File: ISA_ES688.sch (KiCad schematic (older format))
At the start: 106 parts, among them J1 LINE IN, J11 ISA BUS, J2 LINE OUT, J3 Joystick/MIDI, J7 SPKR OUT, J8 MIC, U1 L78L05, U2 74LS14, U7 LM1877, Y1 14.318Mhz

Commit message: Completed OPAMP circuit?
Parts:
- added C28: 5nF, Capacitor_THT:C_Disc_D6.0mm_W2.5mm_P5.00mm, symbol Device:C_Small
- added C29: 2.7nF, Capacitor_THT:C_Disc_D6.0mm_W2.5mm_P5.00mm, symbol Device:C_Small
- added R2, R3: 10k, Resistor_THT:R_Axial_DIN0207_L6.3mm_D2.5mm_P7.62mm_Horizontal, symbol Device:R_Small
- added R4: 2.2k, Resistor_THT:R_Axial_DIN0207_L6.3mm_D2.5mm_P7.62mm_Horizontal, symbol Device:R_Small
- gave numbers to parts that had none: 1
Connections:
- net GNDA: now also C28.2, C29.2
- net MUS_L: now also C28.1, R4.2
- net YAC_CH2: now also U?.10 (IN+), C29.1
- net YAC_MP: now also R6.2, R3.2; no longer R6.1
- net at U?.8 (OUT): now also R2.1, R4.1
- net at U?.9 (IN-): now also R2.2, R3.1
- net at R5.2, U?.13 (IN-): now also R6.1; no longer R6.2
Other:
- moved on the sheet: C26, R1, R6, U?B, U?C
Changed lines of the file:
@@
 L custom_components:LM3403 U?
 U 2 1 618ABB59
-P 19950 11550
-F 0 "U?" H 19750 11850 50  0000 L CNN
-F 1 "LM3403" H 19950 11850 50  0000 L CNN
-F 2 "" H 19950 11550 50  0001 C CNN
-F 3 "" H 19950 11550 50  0001 C CNN
-	2    19950 11550
+P 19950 13500
+F 0 "U?" H 19750 13800 50  0000 L CNN
+F 1 "LM3403" H 19950 13800 50  0000 L CNN
+F 2 "" H 19950 13500 50  0001 C CNN
+F 3 "" H 19950 13500 50  0001 C CNN
+	2    19950 13500
 	1    0    0    -1
 $EndComp
@@
 L custom_components:LM3403 U?
 U 3 1 6191F91E
-P 19950 12500
-F 0 "U?" H 19750 12800 50  0000 L CNN
-F 1 "LM3403" H 19950 12800 50  0000 L CNN
-F 2 "" H 19950 12500 50  0001 C CNN
-F 3 "" H 19950 12500 50  0001 C CNN
-	3    19950 12500
-	1    0    0    -1
+P 19900 11400
+F 0 "U?" H 19700 11700 50  0000 L CNN
+F 1 "LM3403" H 19900 11700 50  0000 L CNN
+F 2 "" H 19900 11400 50  0001 C CNN
+F 3 "" H 19900 11400 50  0001 C CNN
+	3    19900 11400
+	1    0    0    1
 $EndComp
 Text Label 18400 8750 2    50   ~ 0
@@
 L Device:R_Small R6
 U 1 1 620F0F7D
-P 20600 9250
-F 0 "R6" V 20700 9200 50  0000 L CNN
-F 1 "10k" V 20500 9200 50  0000 L CNN
-F 2 "Resistor_THT:R_Axial_DIN0207_L6.3mm_D2.5mm_P7.62mm_Horizontal" H 20600 9250 50  0001 C CNN
-F 3 "~" H 20600 9250 50  0001 C CNN
-	1    20600 9250
-	0    -1   -1   0
-$EndComp
-Wire Wire Line
-	20500 9250 20350 9250
+P 21250 9650
+F 0 "R6" V 21350 9600 50  0000 L CNN
+F 1 "10k" V 21150 9600 50  0000 L CNN
+F 2 "Resistor_THT:R_Axial_DIN0207_L6.3mm_D2.5mm_P7.62mm_Horizontal" H 21250 9650 50  0001 C CNN
+F 3 "~" H 21250 9650 50  0001 C CNN
+	1    21250 9650
+	0    -1   -1   0
+$EndComp
 Connection ~ 20350 9250
-Wire Wire Line
-	20700 9250 20900 9250
-Wire Wire Line
-	20900 9250 20900 9650
 Wire Wire Line
 	20900 9650 19500 9650
@@
 Wire Wire Line
 	20900 9950 20700 9950
-Connection ~ 20900 9650
 $Comp
 L Device:R_Small R7
@@
 C24 measured out of circuit as 160nF
 $Comp
-L Device:C_Small C?
+L Device:C_Small C27
 U 1 1 61F8B525
 P 13100 2950
-F 0 "C?" V 13050 3000 50  0000 L CNN
+F 0 "C27" V 13050 3000 50  0000 L CNN
 F 1 "220nF" V 13050 2650 50  0000 L CNN
 F 2 "Capacitor_THT:C_Disc_D6.0mm_W2.5mm_P5.00mm" H 13100 2950 50  0001 C CNN
@@
 Text Label 18400 8600 2    50   ~ 0
 YAC_AOUT
-Text Label 18950 11450 0    50   ~ 0
+Text Label 18950 13400 0    50   ~ 0
 YAC_AOUT
 Wire Wire Line
-	18950 11450 19500 11450
+	18950 13400 19500 13400
 $Comp
 L Device:C_Small C26
 U 1 1 62A2E09E
-P 19500 11200
-F 0 "C26" H 19550 11300 50  0000 L CNN
-F 1 "33-68pF" H 19550 11100 50  0000 L CNN
-F 2 "Capacitor_THT:C_Disc_D6.0mm_W2.5mm_P5.00mm" H 19500 11200 50  0001 C CNN
-F 3 "~" H 19500 11200 50  0001 C CNN
-	1    19500 11200
+P 19500 13150
+F 0 "C26" H 19550 13250 50  0000 L CNN
+F 1 "33-68pF" H 19550 13050 50  0000 L CNN
+F 2 "Capacitor_THT:C_Disc_D6.0mm_W2.5mm_P5.00mm" H 19500 13150 50  0001 C CNN
+F 3 "~" H 19500 13150 50  0001 C CNN
+	1    19500 13150
 	-1   0    0    -1
 $EndComp
 Wire Wire Line
-	19500 11300 19500 11450
-Connection ~ 19500 11450
-Wire Wire Line
-	19500 11450 19650 11450
+	19500 13250 19500 13400
+Connection ~ 19500 13400
+Wire Wire Line
+	19500 13400 19650 13400
 $Comp
 L power:GNDA #PWR?
 U 1 1 62AAAABD
-P 19150 11000
-F 0 "#PWR?" H 19150 10750 50  0001 C CNN
-F 1 "GNDA" H 19150 10850 50  0000 C CNN
-F 2 "" H 19150 11000 50  0001 C CNN
-F 3 "" H 19150 11000 50  0001 C CNN
-	1    19150 11000
-	1    0    0    -1
-$EndComp
-Wire Wire Line
-	19500 11100 19500 10850
-Wire Wire Line
-	19500 10850 19150 10850
-Wire Wire Line
-	19150 10850 19150 11000
-Wire Wire Line
-	20300 11550 20500 11550
-Wire Wire Line
-	20500 11550 20500 11900
-Wire Wire Line
-	20500 11900 19500 11900
-Wire Wire Line
-	19500 11900 19500 11650
-Wire Wire Line
-	19500 11650 19650 11650
+P 19150 12950
+F 0 "#PWR?" H 19150 12700 50  0001 C CNN
+F 1 "GNDA" H 19150 12800 50  0000 C CNN
+F 2 "" H 19150 12950 50  0001 C CNN
+F 3 "" H 19150 12950 50  0001 C CNN
+	1    19150 12950
+	1    0    0    -1
+$EndComp
+Wire Wire Line
+	19500 13050 19500 12800
+Wire Wire Line
+	19500 12800 19150 12800
+Wire Wire Line
+	19150 12800 19150 12950
+Wire Wire Line
+	20300 13500 20500 13500
+Wire Wire Line
+	20500 13500 20500 13850
+Wire Wire Line
+	20500 13850 19500 13850
+Wire Wire Line
+	19500 13850 19500 13600
+Wire Wire Line
+	19500 13600 19650 13600
 $Comp
 L Device:R_Small R1
 U 1 1 62CA2E14
-P 19400 11650
-F 0 "R1" V 19500 11600 50  0000 L CNN
-F 1 "33" V 19300 11600 50  0000 L CNN
-F 2 "Resistor_THT:R_Axial_DIN0207_L6.3mm_D2.5mm_P7.62mm_Horizontal" H 19400 11650 50  0001 C CNN
-F 3 "~" H 19400 11650 50  0001 C CNN
-	1    19400 11650
-	0    -1   -1   0
-$EndComp
-Connection ~ 19500 11650
-Wire Wire Line
-	19300 11650 18950 11650
-Text Label 18950 11650 0    50   ~ 0
+P 19400 13600
+F 0 "R1" V 19500 13550 50  0000 L CNN
+F 1 "33" V 19300 13550 50  0000 L CNN
+F 2 "Resistor_THT:R_Axial_DIN0207_L6.3mm_D2.5mm_P7.62mm_Horizontal" H 19400 13600 50  0001 C CNN
+F 3 "~" H 19400 13600 50  0001 C CNN
+	1    19400 13600
+	0    -1   -1   0
+$EndComp
+Connection ~ 19500 13600
+Wire Wire Line
+	19300 13600 18950 13600
+Text Label 18950 13600 0    50   ~ 0
 YAC_SWIN
 Wire Wire Line
@@
 Text Label 18400 8300 2    50   ~ 0
 YAC_CH2
+Text Label 19250 11500 0    50   ~ 0
+YAC_CH2
+$Comp
+L Device:C_Small C29
+U 1 1 630238A6
+P 19250 11700
+F 0 "C29" H 19300 11800 50  0000 L CNN
+F 1 "2.7nF" H 19300 11600 50  0000 L CNN
+F 2 "Capacitor_THT:C_Disc_D6.0mm_W2.5mm_P5.00mm" H 19250 11700 50  0001 C CNN
+F 3 "~" H 19250 11700 50  0001 C CNN
+	1    19250 11700
+	-1   0    0    -1
+$EndComp
+$Comp
+L power:GNDA #PWR?
+U 1 1 630238B0
+P 19250 11900
+F 0 "#PWR?" H 19250 11650 50  0001 C CNN
+F 1 "GNDA" H 19400 11850 50  0000 C CNN
+F 2 "" H 19250 11900 50  0001 C CNN
+F 3 "" H 19250 11900 50  0001 C CNN
+	1    19250 11900
+	1    0    0    -1
+$EndComp
+Wire Wire Line
+	19250 11800 19250 11900
+Wire Wire Line
+	19250 11500 19600 11500
+Wire Wire Line
+	19250 11500 19250 11600
+$Comp
+L Device:R_Small R2
+U 1 1 630A4037
+P 20650 11400
+F 0 "R2" V 20750 11350 50  0000 L CNN
+F 1 "10k" V 20550 11350 50  0000 L CNN
+F 2 "Resistor_THT:R_Axial_DIN0207_L6.3mm_D2.5mm_P7.62mm_Horizontal" H 20650 11400 50  0001 C CNN
+F 3 "~" H 20650 11400 50  0001 C CNN
+	1    20650 11400
+	0    -1   -1   0
+$EndComp
+Wire Wire Line
+	20250 11400 20350 11400
+Wire Wire Line
+	20950 11100 20950 11400
+Wire Wire Line
+	20950 11400 20750 11400
+$Comp
+L Device:R_Small R4
+U 1 1 630A51B2
+P 20650 11700
+F 0 "R4" V 20750 11650 50  0000 L CNN
+F 1 "2.2k" V 20550 11650 50  0000 L CNN
+F 2 "Resistor_THT:R_Axial_DIN0207_L6.3mm_D2.5mm_P7.62mm_Horizontal" H 20650 11700 50  0001 C CNN
+F 3 "~" H 20650 11700 50  0001 C CNN
+	1    20650 11700
+	0    -1   -1   0
+$EndComp
+Wire Wire Line
+	20350 11400 20350 11700
+Wire Wire Line
+	20350 11700 20550 11700
+Connection ~ 20350 11400
+Wire Wire Line
+	20350 11400 20550 11400
+$Comp
+L Device:C_Small C28
+U 1 1 630A51C0
+P 20950 11900
+F 0 "C28" H 21050 11900 50  0000 L CNN
+F 1 "5nF" H 21000 11800 50  0000 L CNN
+F 2 "Capacitor_THT:C_Disc_D6.0mm_W2.5mm_P5.00mm" H 20950 11900 50  0001 C CNN
+F 3 "~" H 20950 11900 50  0001 C CNN
+	1    20950 11900
+	-1   0    0    -1
+$EndComp
+Wire Wire Line
+	20750 11700 20950 11700
+Wire Wire Line
+	20950 11700 20950 11800
+$Comp
+L power:GNDA #PWR?
+U 1 1 630A51CC
+P 20950 12050
+F 0 "#PWR?" H 20950 11800 50  0001 C CNN
+F 1 "GNDA" H 21100 12000 50  0000 C CNN
+F 2 "" H 20950 12050 50  0001 C CNN
+F 3 "" H 20950 12050 50  0001 C CNN
+	1    20950 12050
+	1    0    0    -1
+$EndComp
+Wire Wire Line
+	20950 12000 20950 12050
+Text Label 21400 11700 2    50   ~ 0
+MUS_L
+Wire Wire Line
+	20950 11700 21400 11700
+Connection ~ 20950 11700
+Wire Wire Line
+	20950 11100 19500 11100
+Wire Wire Line
+	19500 11100 19500 11300
+Wire Wire Line
+	19500 11300 19600 11300
+Wire Wire Line
+	20900 9650 21150 9650
+Connection ~ 20900 9650
+Wire Wire Line
+	21350 9650 21550 9650
+Wire Wire Line
+	21550 9650 21550 9250
+Wire Wire Line
+	20350 9250 21550 9250
+$Comp
+L Device:R_Small R3
+U 1 1 6333896F
+P 21250 11100
+F 0 "R3" V 21350 11050 50  0000 L CNN
+F 1 "10k" V 21150 11050 50  0000 L CNN
+F 2 "Resistor_THT:R_Axial_DIN0207_L6.3mm_D2.5mm_P7.62mm_Horizontal" H 21250 11100 50  0001 C CNN
+F 3 "~" H 21250 11100 50  0001 C CNN
+	1    21250 11100
+	0    -1   -1   0
+$EndComp
+Wire Wire Line
+	21150 11100 20950 11100
+Connection ~ 20950 11100
+Wire Wire Line
+	21550 9650 21550 11100
+Wire Wire Line
+	21550 11100 21350 11100
+Connection ~ 21550 9650
 $EndSCHEMATC

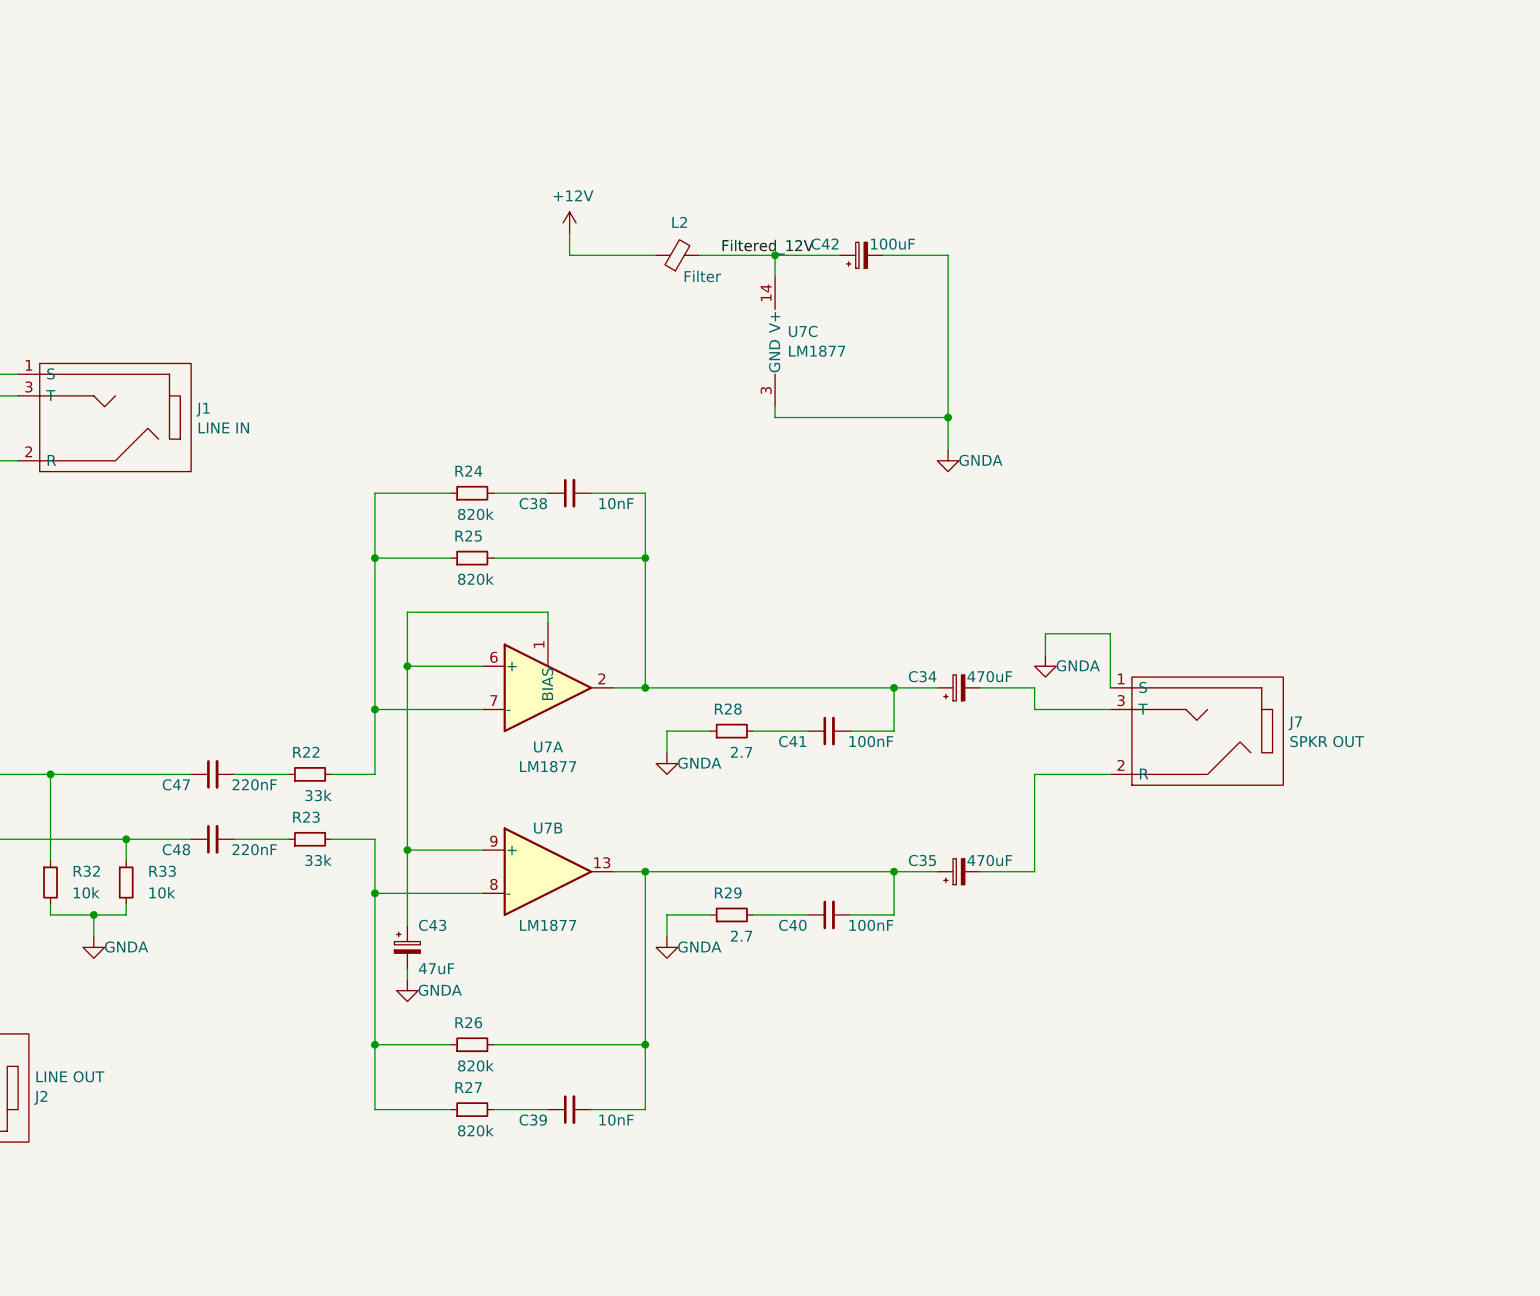
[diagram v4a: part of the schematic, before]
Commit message: Add volume pot footprint, and volume control to sch
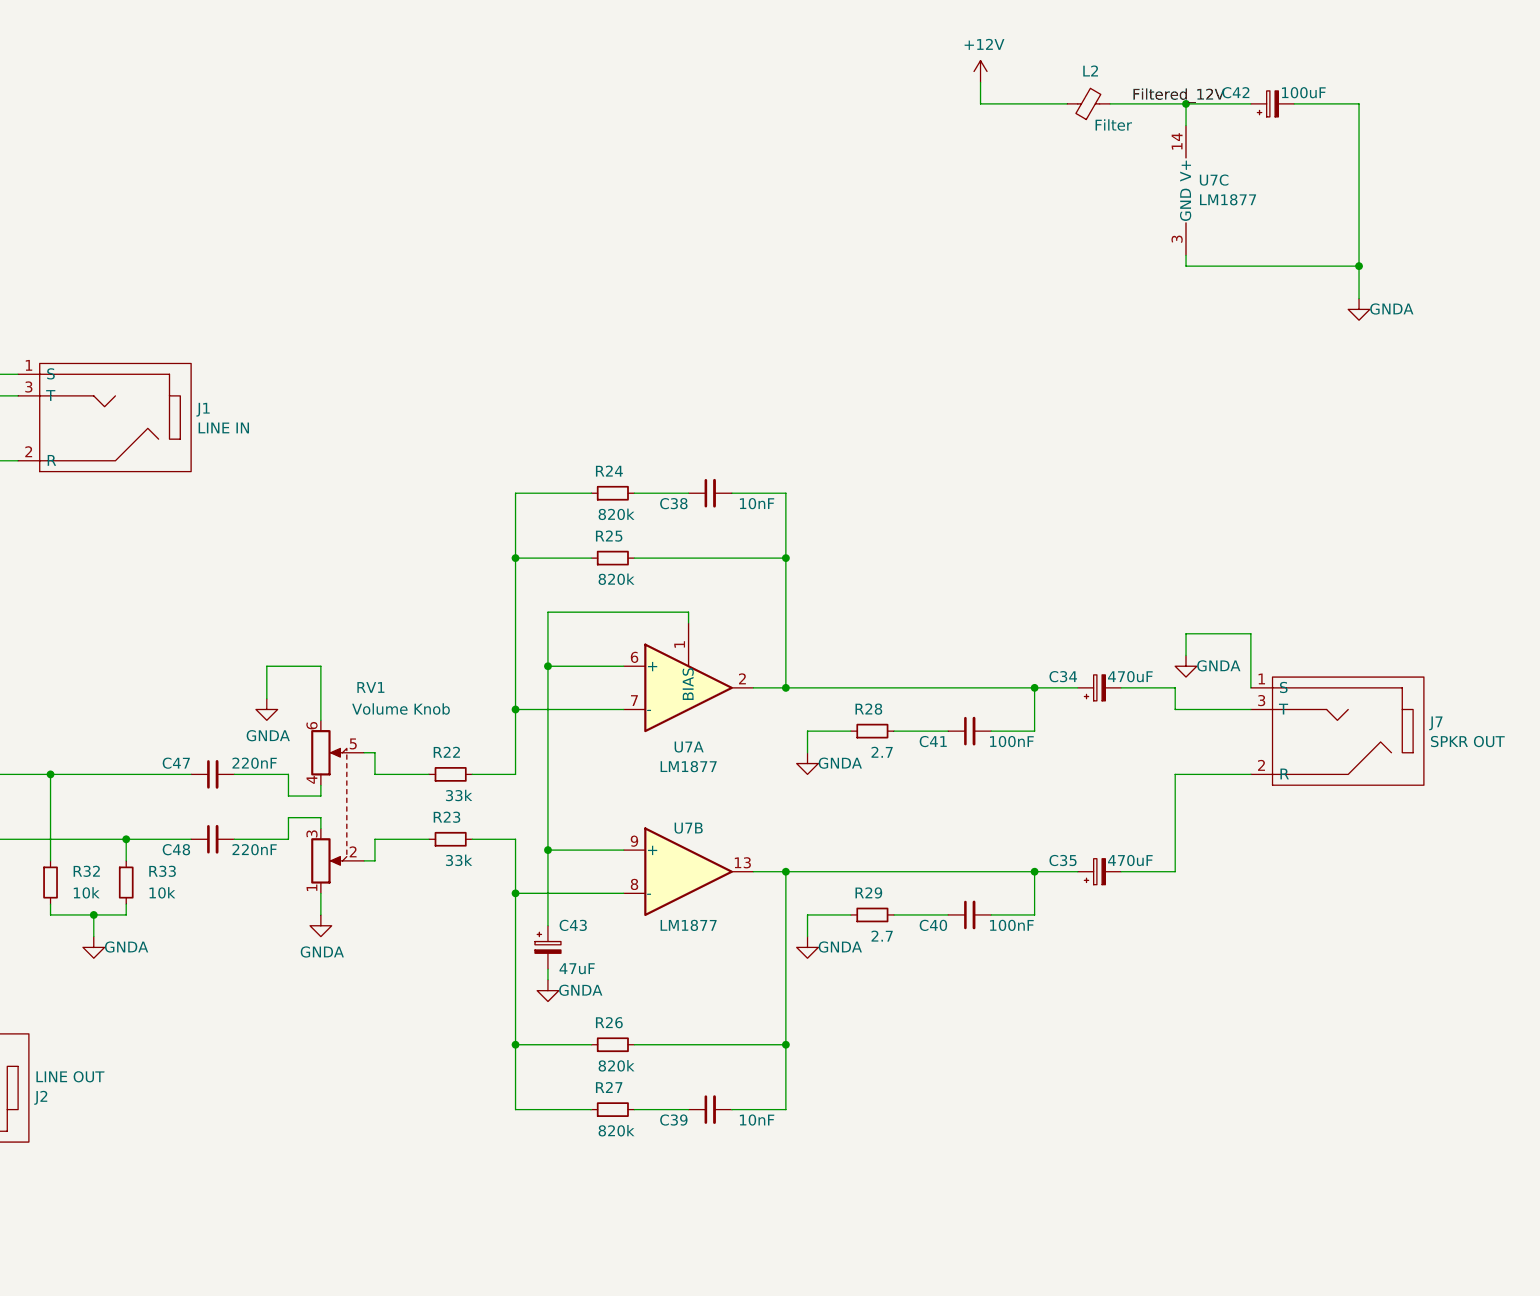
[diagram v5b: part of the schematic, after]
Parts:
- added RV1: Volume Knob, symbol Device:R_POT_Dual
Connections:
- net GNDA: now also RV1.1, RV1.6
- net at C47.2: now also RV1.4; no longer R22.1
- net at C48.2: now also RV1.3; no longer R23.1
- new net: R22.1, RV1.5
- new net: R23.1, RV1.2
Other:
- moved on the sheet: C34, C35, C38, C39, C40, C41, C42, C43, J7, L2, R22, R23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
